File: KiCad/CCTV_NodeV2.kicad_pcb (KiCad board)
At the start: 2 copper layers, 100 x 80 mm, 9 parts, among them J1 SOLAR, J2 BATT, U1 CN3791, U2 BMS 1S, U3 MT3608, U4 ESP32-S3, U5 OV7670

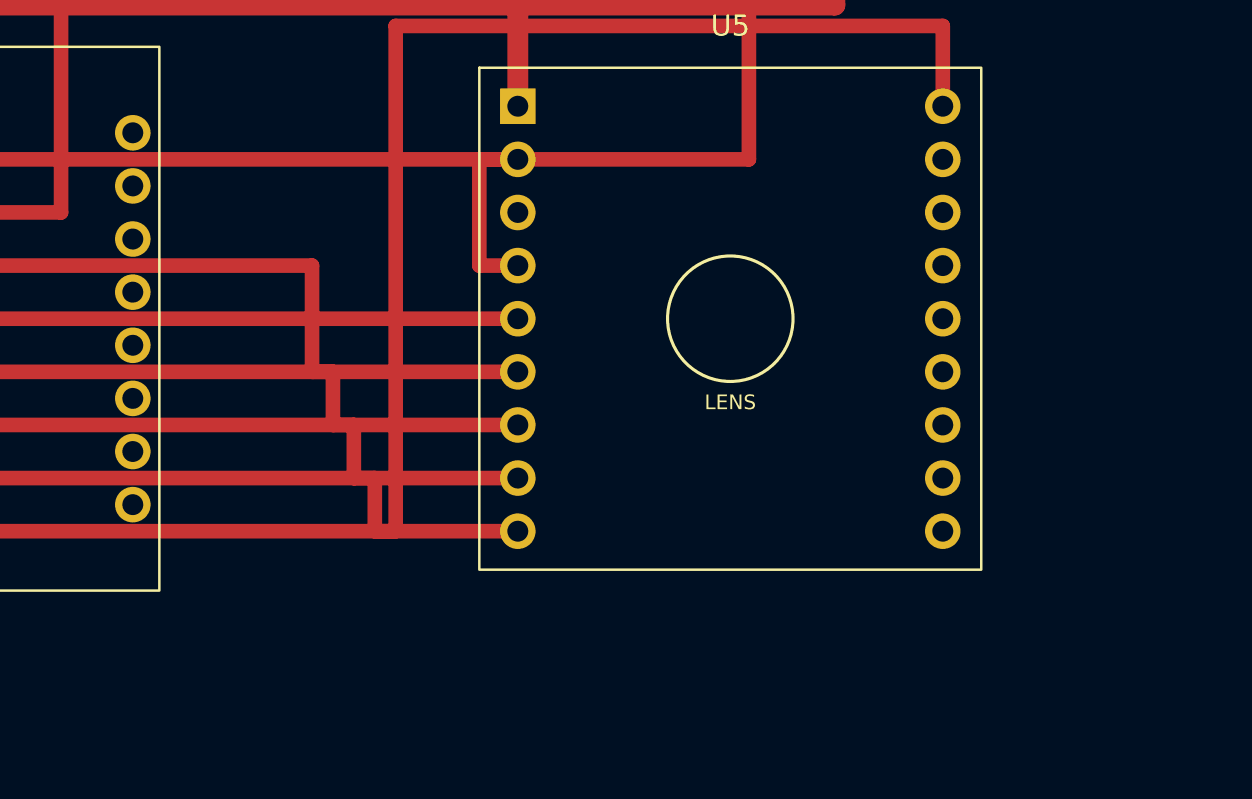
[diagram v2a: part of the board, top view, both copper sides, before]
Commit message: Route CAM_D0..D3 on B.Cu (data lines 0-3 of camera bus)
Each line uses 5 segments on B.Cu (back copper) so they cross
underneath the existing F.Cu power and control traces without
conflict. All traces 0.7mm width.

Pattern per line: U4 right pad -> exit east -> south to bottom rail
in the y=68-71 area -> east past OV7670 right edge -> north up to
target y -> west into U5 right pad.

D0: rail y=68,   exit x=44,   approach x=85   (U4.10 y=46.11 -> U5.18 y=65.16)
D1: rail y=69.2, exit x=45.2, approach x=86.2 (U4.11 y=48.65 -> U5.17 y=62.62)
D2: rail y=70.4, exit x=46.4, approach x=87.4 (U4.12 y=51.19 -> U5.16 y=60.08)
D3: rail y=71.6, exit x=47.6, approach x=88.6 (U4.13 y=53.73 -> U5.15 y=57.54)

Verticals at exit_x and approach_x are 1.2mm apart, well clear of
0.7mm trace + 0.2mm clearance.

Next batch: D4-D7 (the lines going the other direction, from U4
bottom rows to U5 top rows).
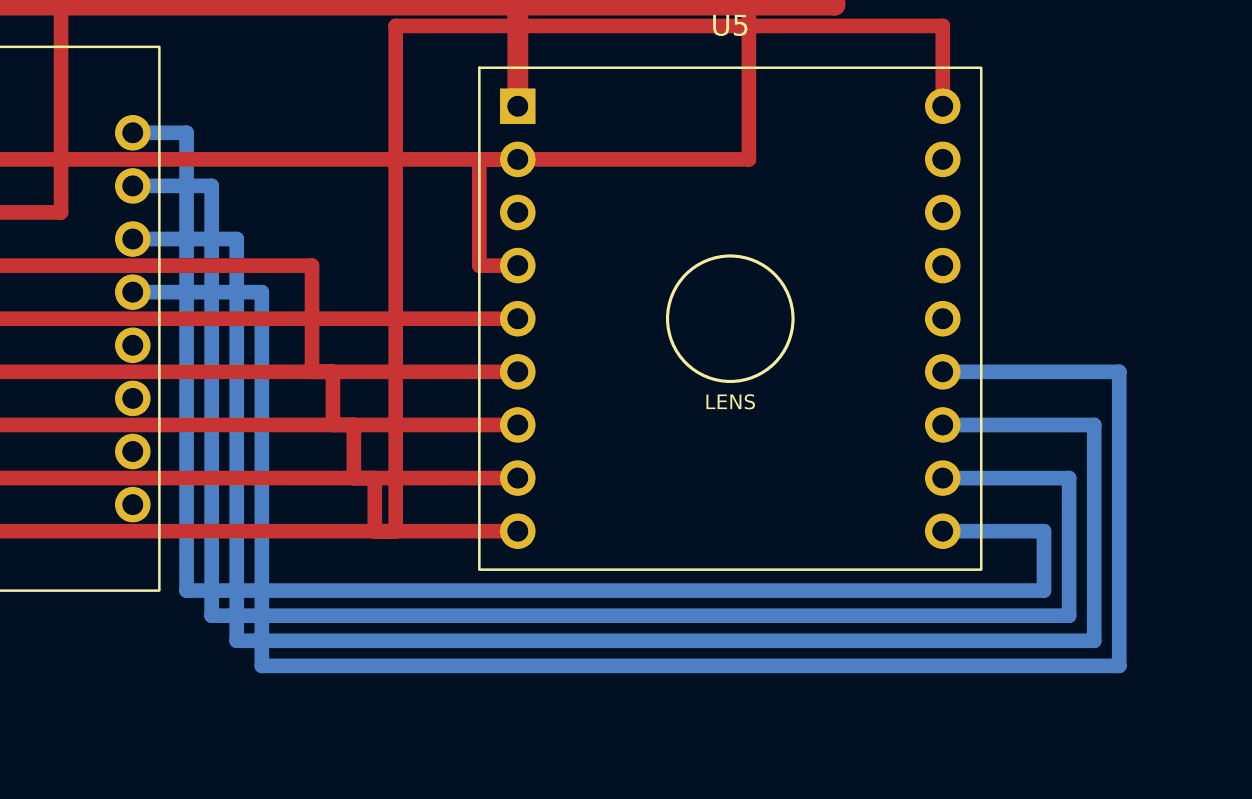
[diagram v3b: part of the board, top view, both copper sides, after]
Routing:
- net CAM_D3: track 0.00 -> 87.5 mm
- net CAM_D2: track 0.00 -> 82.7 mm
- net CAM_D1: track 0.00 -> 77.9 mm
- net CAM_D0: track 0.00 -> 73.1 mm
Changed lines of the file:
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@@
 	(segment (start 58 52.46) (end 59.84 52.46) (width 0.7) (layer "F.Cu") (net 5) (uuid "trace0037-0000-0000-0000-000000000037"))
 	(segment (start 18.57 47.38) (end 59.84 47.38) (width 0.7) (layer "F.Cu") (net 5) (uuid "trace0038-0000-0000-0000-000000000038"))
+	(segment (start 41.43 46.11) (end 44 46.11) (width 0.7) (layer "B.Cu") (net 14) (uuid "trace0039-0000-0000-0000-000000000039"))
+	(segment (start 44 46.11) (end 44 68) (width 0.7) (layer "B.Cu") (net 14) (uuid "trace003a-0000-0000-0000-00000000003a"))
+	(segment (start 44 68) (end 85 68) (width 0.7) (layer "B.Cu") (net 14) (uuid "trace003b-0000-0000-0000-00000000003b"))
+	(segment (start 85 68) (end 85 65.16) (width 0.7) (layer "B.Cu") (net 14) (uuid "trace003c-0000-0000-0000-00000000003c"))
+	(segment (start 85 65.16) (end 80.16 65.16) (width 0.7) (layer "B.Cu") (net 14) (uuid "trace003d-0000-0000-0000-00000000003d"))
+	(segment (start 41.43 48.65) (end 45.2 48.65) (width 0.7) (layer "B.Cu") (net 15) (uuid "trace003e-0000-0000-0000-00000000003e"))
+	(segment (start 45.2 48.65) (end 45.2 69.2) (width 0.7) (layer "B.Cu") (net 15) (uuid "trace003f-0000-0000-0000-00000000003f"))
+	(segment (start 45.2 69.2) (end 86.2 69.2) (width 0.7) (layer "B.Cu") (net 15) (uuid "trace0040-0000-0000-0000-000000000040"))
+	(segment (start 86.2 69.2) (end 86.2 62.62) (width 0.7) (layer "B.Cu") (net 15) (uuid "trace0041-0000-0000-0000-000000000041"))
+	(segment (start 86.2 62.62) (end 80.16 62.62) (width 0.7) (layer "B.Cu") (net 15) (uuid "trace0042-0000-0000-0000-000000000042"))
+	(segment (start 41.43 51.19) (end 46.4 51.19) (width 0.7) (layer "B.Cu") (net 16) (uuid "trace0043-0000-0000-0000-000000000043"))
+	(segment (start 46.4 51.19) (end 46.4 70.4) (width 0.7) (layer "B.Cu") (net 16) (uuid "trace0044-0000-0000-0000-000000000044"))
+	(segment (start 46.4 70.4) (end 87.4 70.4) (width 0.7) (layer "B.Cu") (net 16) (uuid "trace0045-0000-0000-0000-000000000045"))
+	(segment (start 87.4 70.4) (end 87.4 60.08) (width 0.7) (layer "B.Cu") (net 16) (uuid "trace0046-0000-0000-0000-000000000046"))
+	(segment (start 87.4 60.08) (end 80.16 60.08) (width 0.7) (layer "B.Cu") (net 16) (uuid "trace0047-0000-0000-0000-000000000047"))
+	(segment (start 41.43 53.73) (end 47.6 53.73) (width 0.7) (layer "B.Cu") (net 17) (uuid "trace0048-0000-0000-0000-000000000048"))
+	(segment (start 47.6 53.73) (end 47.6 71.6) (width 0.7) (layer "B.Cu") (net 17) (uuid "trace0049-0000-0000-0000-000000000049"))
+	(segment (start 47.6 71.6) (end 88.6 71.6) (width 0.7) (layer "B.Cu") (net 17) (uuid "trace004a-0000-0000-0000-00000000004a"))
+	(segment (start 88.6 71.6) (end 88.6 57.54) (width 0.7) (layer "B.Cu") (net 17) (uuid "trace004b-0000-0000-0000-00000000004b"))
+	(segment (start 88.6 57.54) (end 80.16 57.54) (width 0.7) (layer "B.Cu") (net 17) (uuid "trace004c-0000-0000-0000-00000000004c"))
 	(embedded_fonts no)
 )

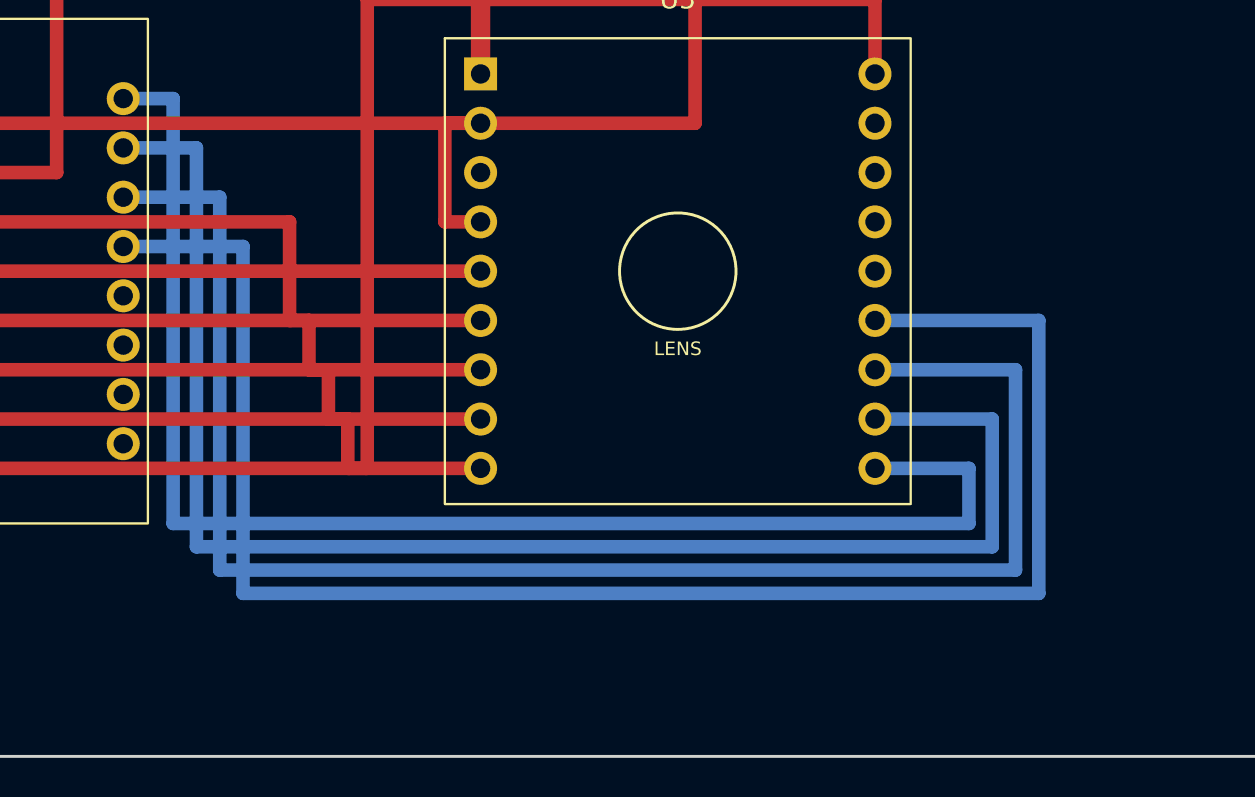
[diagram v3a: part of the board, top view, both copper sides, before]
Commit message: Route CAM_D4..D7 on B.Cu (data lines 4-7 of camera bus, completes board)
D4: rail y=72.8, exit x=48.8, approach x=89.8 (U4.14 y=56.27 -> U5.14 y=55)
D5: rail y=74,   exit x=50,   approach x=91   (U4.15 y=58.81 -> U5.13 y=52.46)
D6: rail y=75.2, exit x=51.2, approach x=92.2 (U4.16 y=61.35 -> U5.12 y=49.92)
D7: rail y=76.4, exit x=52.4, approach x=93.4 (U4.17 y=63.89 -> U5.11 y=47.38)

Board now has 96 trace segments total. Every net in the ratsnest
should be cleared after pressing B in pcbnew.
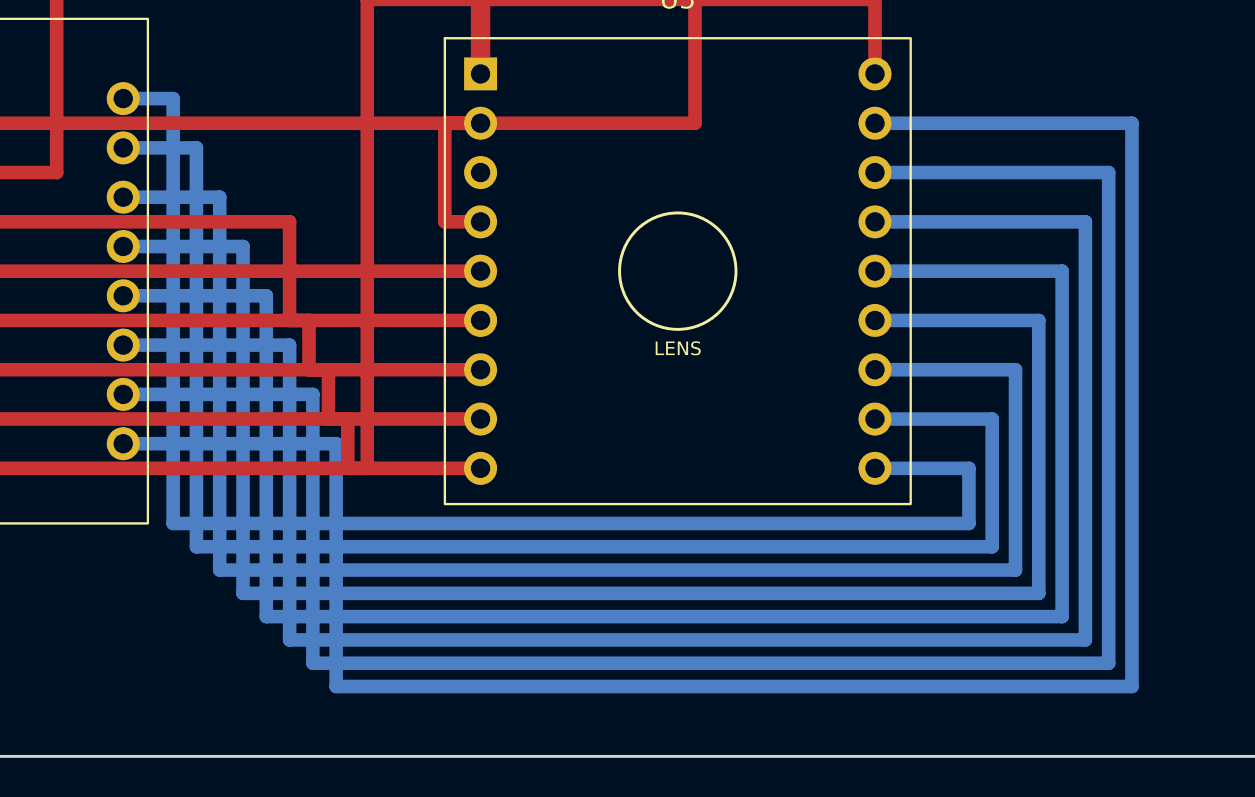
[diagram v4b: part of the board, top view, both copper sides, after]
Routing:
- net CAM_D7: track 0.00 -> 106.7 mm
- net CAM_D6: track 0.00 -> 101.9 mm
- net CAM_D5: track 0.00 -> 97.1 mm
- net CAM_D4: track 0.00 -> 92.3 mm
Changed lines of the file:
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@@
 	(segment (start 88.6 71.6) (end 88.6 57.54) (width 0.7) (layer "B.Cu") (net 17) (uuid "trace004b-0000-0000-0000-00000000004b"))
 	(segment (start 88.6 57.54) (end 80.16 57.54) (width 0.7) (layer "B.Cu") (net 17) (uuid "trace004c-0000-0000-0000-00000000004c"))
+	(segment (start 41.43 56.27) (end 48.8 56.27) (width 0.7) (layer "B.Cu") (net 18) (uuid "trace004d-0000-0000-0000-00000000004d"))
+	(segment (start 48.8 56.27) (end 48.8 72.8) (width 0.7) (layer "B.Cu") (net 18) (uuid "trace004e-0000-0000-0000-00000000004e"))
+	(segment (start 48.8 72.8) (end 89.8 72.8) (width 0.7) (layer "B.Cu") (net 18) (uuid "trace004f-0000-0000-0000-00000000004f"))
+	(segment (start 89.8 72.8) (end 89.8 55) (width 0.7) (layer "B.Cu") (net 18) (uuid "trace0050-0000-0000-0000-000000000050"))
+	(segment (start 89.8 55) (end 80.16 55) (width 0.7) (layer "B.Cu") (net 18) (uuid "trace0051-0000-0000-0000-000000000051"))
+	(segment (start 41.43 58.81) (end 50 58.81) (width 0.7) (layer "B.Cu") (net 19) (uuid "trace0052-0000-0000-0000-000000000052"))
+	(segment (start 50 58.81) (end 50 74) (width 0.7) (layer "B.Cu") (net 19) (uuid "trace0053-0000-0000-0000-000000000053"))
+	(segment (start 50 74) (end 91 74) (width 0.7) (layer "B.Cu") (net 19) (uuid "trace0054-0000-0000-0000-000000000054"))
+	(segment (start 91 74) (end 91 52.46) (width 0.7) (layer "B.Cu") (net 19) (uuid "trace0055-0000-0000-0000-000000000055"))
+	(segment (start 91 52.46) (end 80.16 52.46) (width 0.7) (layer "B.Cu") (net 19) (uuid "trace0056-0000-0000-0000-000000000056"))
+	(segment (start 41.43 61.35) (end 51.2 61.35) (width 0.7) (layer "B.Cu") (net 20) (uuid "trace0057-0000-0000-0000-000000000057"))
+	(segment (start 51.2 61.35) (end 51.2 75.2) (width 0.7) (layer "B.Cu") (net 20) (uuid "trace0058-0000-0000-0000-000000000058"))
+	(segment (start 51.2 75.2) (end 92.2 75.2) (width 0.7) (layer "B.Cu") (net 20) (uuid "trace0059-0000-0000-0000-000000000059"))
+	(segment (start 92.2 75.2) (end 92.2 49.92) (width 0.7) (layer "B.Cu") (net 20) (uuid "trace005a-0000-0000-0000-00000000005a"))
+	(segment (start 92.2 49.92) (end 80.16 49.92) (width 0.7) (layer "B.Cu") (net 20) (uuid "trace005b-0000-0000-0000-00000000005b"))
+	(segment (start 41.43 63.89) (end 52.4 63.89) (width 0.7) (layer "B.Cu") (net 21) (uuid "trace005c-0000-0000-0000-00000000005c"))
+	(segment (start 52.4 63.89) (end 52.4 76.4) (width 0.7) (layer "B.Cu") (net 21) (uuid "trace005d-0000-0000-0000-00000000005d"))
+	(segment (start 52.4 76.4) (end 93.4 76.4) (width 0.7) (layer "B.Cu") (net 21) (uuid "trace005e-0000-0000-0000-00000000005e"))
+	(segment (start 93.4 76.4) (end 93.4 47.38) (width 0.7) (layer "B.Cu") (net 21) (uuid "trace005f-0000-0000-0000-00000000005f"))
+	(segment (start 93.4 47.38) (end 80.16 47.38) (width 0.7) (layer "B.Cu") (net 21) (uuid "trace0060-0000-0000-0000-000000000060"))
 	(embedded_fonts no)
 )
